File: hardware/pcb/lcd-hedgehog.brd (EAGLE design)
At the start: 24.4 x 27.4 mm, 40 parts

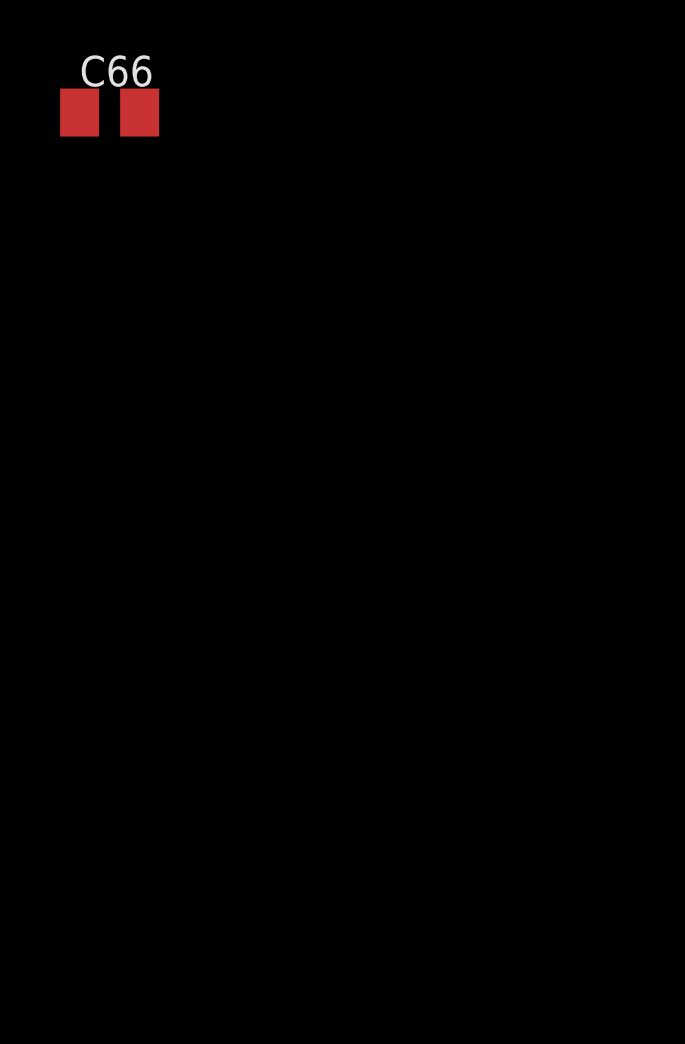
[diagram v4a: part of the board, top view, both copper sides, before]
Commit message: added 12V power circuit2
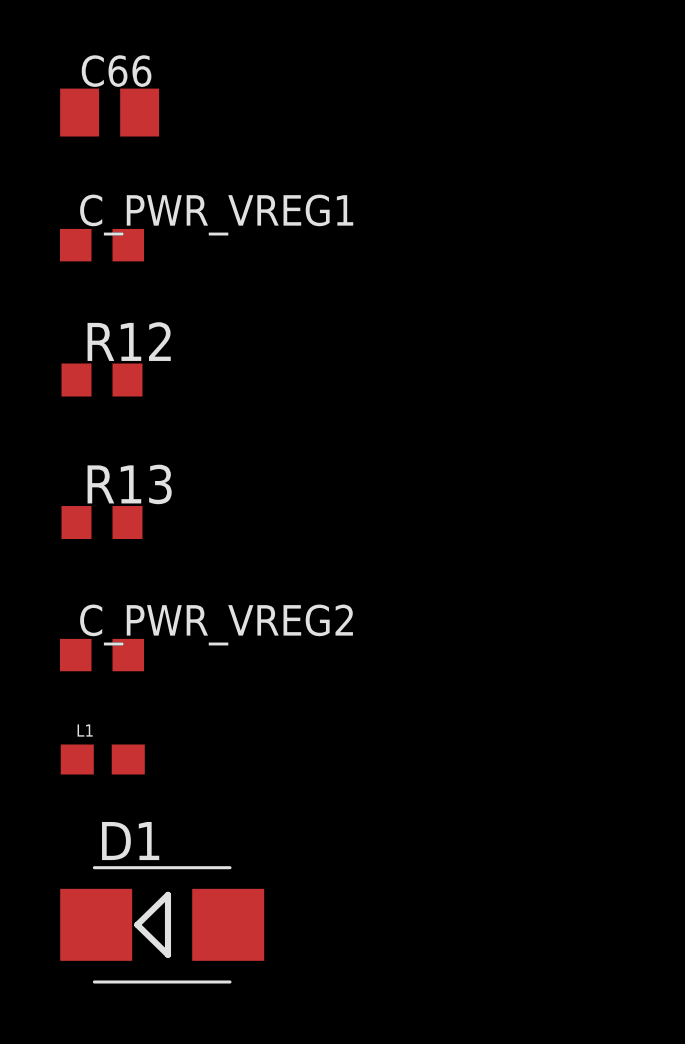
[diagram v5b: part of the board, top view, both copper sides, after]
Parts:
- added C_PWR_VREG1: 4.7uF, rcl:C0603K
- added C_PWR_VREG2: 1uF/12V, rcl:C0603K
- added D1: MBRS130LT3, diode:SMB
- added L1: 10uH, jnode:SPARKFUN_0603
- added R12: 27k, rcl:R0603
- added R13: 240k, rcl:R0603
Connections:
- new net 12V: C_PWR_VREG2.1, D1.C, R13.2, U$4.P$22
- new net N$15: R12.2, R13.1, U$5.3
- new net N$16: D1.A, L1.1, U$5.1
- net +3V3: now also C_PWR_VREG1.1, L1.2, U$5.4, U$5.5
- net GND: now also C_PWR_VREG1.2, C_PWR_VREG2.2, R12.1
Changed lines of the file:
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@@
 <element name="R11" library="rcl" package="R0603" value="20" x="-4.3942" y="-26.543"/>
 <element name="C66" library="rcl" package="C0805K" value="10uF" x="-4.1402" y="-31.1912"/>
+<element name="C_PWR_VREG1" library="rcl" package="C0603K" value="4.7uF" x="-4.3942" y="-35.6108"/>
+<element name="R12" library="rcl" package="R0603" value="27k" x="-4.3942" y="-40.1066"/>
+<element name="R13" library="rcl" package="R0603" value="240k" x="-4.3942" y="-44.8564"/>
+<element name="C_PWR_VREG2" library="rcl" package="C0603K" value="1uF/12V" x="-4.3942" y="-49.276"/>
+<element name="L1" library="jnode" package="SPARKFUN_0603" value="10uH" x="-4.3688" y="-52.7558"/>
+<element name="D1" library="diode" package="SMB" value="MBRS130LT3" x="-2.3876" y="-58.2676"/>
 </elements>
 <signals>
@@
 <contactref element="C64" pad="2"/>
 <contactref element="C66" pad="2"/>
+<contactref element="R12" pad="1"/>
+<contactref element="C_PWR_VREG2" pad="2"/>
+<contactref element="C_PWR_VREG1" pad="2"/>
+<wire x1="54.9402" y1="13.5722" x2="53.6702" y2="13.5722" width="0" layer="19" extent="1-1"/>
+<wire x1="34.1856" y1="16.8462" x2="53.6702" y2="13.5722" width="0" layer="19" extent="1-1"/>
 <wire x1="23.3172" y1="14.6812" x2="34.1856" y2="16.8462" width="0" layer="19" extent="1-1"/>
 <wire x1="19.4004" y1="13.684" x2="23.3172" y2="14.6812" width="0" layer="19" extent="1-1"/>
@@
 <wire x1="2.9808" y1="2.9232" x2="3.2512" y2="5.5786" width="0" layer="19" extent="1-16"/>
 <wire x1="1.524" y1="1.651" x2="2.9808" y2="2.9232" width="0" layer="19" extent="1-16"/>
-<wire x1="53.6702" y1="13.5722" x2="1.524" y2="1.651" width="0" layer="19" extent="1-1"/>
-<wire x1="54.9402" y1="13.5722" x2="53.6702" y2="13.5722" width="0" layer="19" extent="1-1"/>
 <wire x1="23.3473" y1="6.858" x2="19.4004" y2="9.684" width="0" layer="19" extent="1-1"/>
-<wire x1="-3.1402" y1="-17.145" x2="53.6702" y2="13.5722" width="0" layer="19" extent="1-1"/>
+<wire x1="-3.1402" y1="-17.145" x2="1.524" y2="1.651" width="0" layer="19" extent="1-1"/>
 <wire x1="-5.2442" y1="-26.543" x2="-3.1402" y2="-17.145" width="0" layer="19" extent="1-1"/>
 <wire x1="-3.1402" y1="-31.1912" x2="-5.2442" y2="-26.543" width="0" layer="19" extent="1-1"/>
+<wire x1="-3.5192" y1="-35.6108" x2="-3.1402" y2="-31.1912" width="0" layer="19" extent="1-1"/>
+<wire x1="-5.2442" y1="-40.1066" x2="-3.5192" y2="-35.6108" width="0" layer="19" extent="1-1"/>
+<wire x1="-3.5192" y1="-49.276" x2="-5.2442" y2="-40.1066" width="0" layer="19" extent="1-1"/>
 </signal>
 <signal name="D+">
@@
 <contactref element="C66" pad="1"/>
 <contactref element="U$2" pad="P9"/>
+<contactref element="C_PWR_VREG1" pad="1"/>
+<contactref element="U$5" pad="4"/>
+<contactref element="U$5" pad="5"/>
+<contactref element="L1" pad="2"/>
+<wire x1="49.8602" y1="7.4722" x2="54.9402" y2="7.4722" width="0" layer="19" extent="1-1"/>
+<wire x1="34.1856" y1="14.6462" x2="49.8602" y2="7.4722" width="0" layer="19" extent="1-1"/>
 <wire x1="19.4004" y1="14.184" x2="34.1856" y2="14.6462" width="0" layer="19" extent="1-1"/>
 <wire x1="19.4004" y1="9.184" x2="19.4004" y2="14.184" width="0" layer="19" extent="1-1"/>
-<wire x1="18.7604" y1="5.5508" x2="19.4004" y2="9.184" width="0" layer="19" extent="1-16"/>
-<wire x1="20.8026" y1="5.5508" x2="18.7604" y2="5.5508" width="0" layer="19" extent="16-16"/>
+<wire x1="20.7471" y1="7.808" x2="19.4004" y2="9.184" width="0" layer="19" extent="1-1"/>
+<wire x1="20.7471" y1="5.908" x2="20.7471" y2="7.808" width="0" layer="19" extent="1-1"/>
+<wire x1="20.8026" y1="5.5508" x2="20.7471" y2="5.908" width="0" layer="19" extent="1-16"/>
+<wire x1="18.7604" y1="5.5508" x2="20.7471" y2="5.908" width="0" layer="19" extent="1-16"/>
 <wire x1="13.9004" y1="8.184" x2="18.7604" y2="5.5508" width="0" layer="19" extent="1-16"/>
 <wire x1="10.8308" y1="10.9232" x2="13.9004" y2="8.184" width="0" layer="19" extent="1-16"/>
@@
 <wire x1="10.3496" y1="18.5928" x2="6.4262" y2="16.1408" width="0" layer="19" extent="1-1"/>
 <wire x1="8.4074" y1="21.7542" x2="10.3496" y2="18.5928" width="0" layer="19" extent="1-16"/>
-<wire x1="54.9402" y1="7.4722" x2="10.8308" y2="3.7232" width="0" layer="19" extent="1-16"/>
-<wire x1="49.8602" y1="7.4722" x2="54.9402" y2="7.4722" width="0" layer="19" extent="1-1"/>
-<wire x1="-3.5442" y1="-12.4968" x2="49.8602" y2="7.4722" width="0" layer="19" extent="1-1"/>
+<wire x1="-3.5442" y1="-12.4968" x2="0.9652" y2="7.3754" width="0" layer="19" extent="1-1"/>
 <wire x1="-5.1402" y1="-31.1912" x2="-3.5442" y2="-12.4968" width="0" layer="19" extent="1-1"/>
+<wire x1="-5.2692" y1="-35.6108" x2="-5.1402" y2="-31.1912" width="0" layer="19" extent="1-1"/>
+<wire x1="-3.5188" y1="-52.7558" x2="-5.2692" y2="-35.6108" width="0" layer="19" extent="1-1"/>
 </signal>
 <signal name="SDI">
@@
 <wire x1="-3.1402" y1="-21.7932" x2="-3.5442" y2="-26.543" width="0" layer="19" extent="1-1"/>
 </signal>
+<signal name="N$15">
+<contactref element="R12" pad="2"/>
+<contactref element="R13" pad="1"/>
+<contactref element="U$5" pad="3"/>
+<wire x1="-3.5442" y1="-40.1066" x2="-5.2442" y2="-44.8564" width="0" layer="19" extent="1-1"/>
+<wire x1="23.3473" y1="7.808" x2="-3.5442" y2="-40.1066" width="0" layer="19" extent="1-1"/>
+</signal>
+<signal name="12V">
+<contactref element="R13" pad="2"/>
+<contactref element="C_PWR_VREG2" pad="1"/>
+<contactref element="D1" pad="C"/>
+<contactref element="U$4" pad="P$22"/>
+<wire x1="-5.2692" y1="-49.276" x2="-4.5876" y2="-58.2676" width="0" layer="19" extent="1-1"/>
+<wire x1="-3.5442" y1="-44.8564" x2="-5.2692" y2="-49.276" width="0" layer="19" extent="1-1"/>
+<wire x1="6.7856" y1="4.556" x2="-3.5442" y2="-44.8564" width="0" layer="19" extent="1-1"/>
+</signal>
+<signal name="N$16">
+<contactref element="U$5" pad="1"/>
+<contactref element="D1" pad="A"/>
+<contactref element="L1" pad="1"/>
+<wire x1="-5.2188" y1="-52.7558" x2="-0.1876" y2="-58.2676" width="0" layer="19" extent="1-1"/>
+<wire x1="23.3473" y1="5.908" x2="-5.2188" y2="-52.7558" width="0" layer="19" extent="1-1"/>
+</signal>
 </signals>

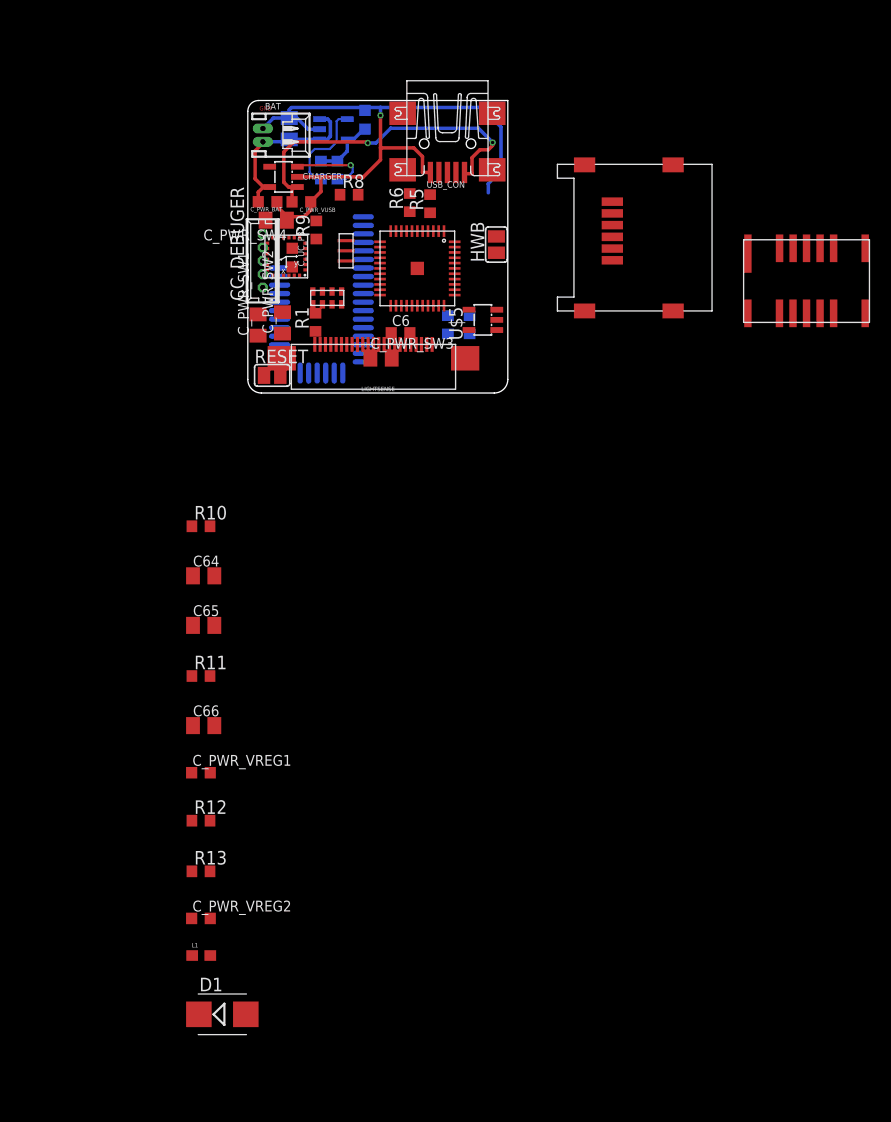
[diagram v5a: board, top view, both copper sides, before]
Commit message: connected Display & first placement
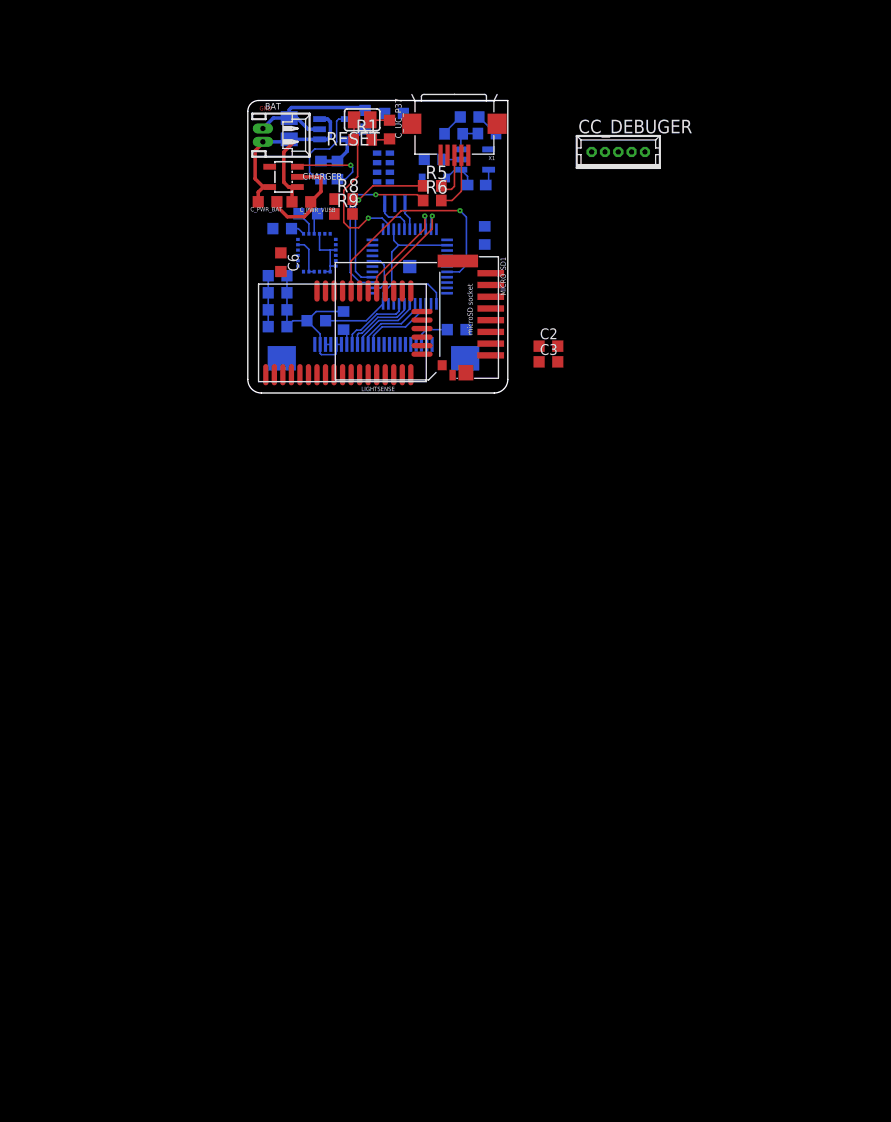
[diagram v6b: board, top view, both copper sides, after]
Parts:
- removed C64: 1.5uF, rcl:C0805K
- removed C65: 1uF, rcl:C0805K
- removed C66: 10uF, rcl:C0805K
- removed C_PWR_SW1, C_PWR_SW2: 10u, rcl:C0805K
- removed C_PWR_SW3: 4.7uF, rcl:C0805K
- removed C_PWR_SW4: 0.22uF, rcl:C0805K
- removed D1: MBRS130LT3, diode:SMB
- removed HWB: (no value), jumper:SJ
- removed R10, R2: 10k, rcl:R0603
- removed R11: 20, rcl:R0603
- removed SDCARD_CON: MICROSD_CONN, HedgehogLib:460DA40013
- removed USB_CON: USBCON, HedgehogLib:248601
- added 1.2M=((VIREF-GND)/IREF): 240k, rcl:R0603
- added C1, C3, C8, C_PWR_VUSB1, C_PWR_VUSB2: 10uF, rcl:C0603K
- added C10: 4.7uF, rcl:C0603K
- added C2, C5, C7: 0.1uF, rcl:C0603K
- added C4: 4.7uF/20V Tantalum CAP, rcl:C0603K
- added C9: 0.22uF, rcl:C0603K
- added MICRO_SD1: TECO_DIV_SENSOR_BOARD_MOLEX_47309-2651NEW, jnode_v32:TECO_DIV_SENSOR_BOARD_MOLEX_47309-2651
- added X1: SPARKFUN_USB-MICROB, jnode_v32:SPARKFUN_USB-MICROB
- U$2: value GRID-EYE -> DIODE-ZENER-BZT52; device HedgehogLib:GRID-EYE -> SparkFun-DiscreteSemi:SOD-323
- moved C_PWR_VREG2 79.3 mm to (20.8, 25.9), flipped to the bottom, turned to 180 degrees
- moved L1 76.7 mm to (21.5, 19.5), flipped to the bottom, turned to 180 degrees
- moved R13 73.1 mm to (19.3, 24.3), flipped to the bottom
- moved R12 69.8 mm to (22.4, 24.3), flipped to the bottom
- moved C_PWR_VREG1 61.5 mm to (17.4, 21.9), flipped to the bottom, turned to 180 degrees
- moved U$2 37.6 mm to (17.5, 20.2), flipped to the bottom, turned to 180 degrees
- moved CC_DEBUGER 34.9 mm to (34.7, 22.6), turned to 0 degrees
- moved RESET 25.4 mm to (10.7, 25.6), turned to 180 degrees
- moved R1 17.7 mm to (10.8, 23.7), turned to 0 degrees
- moved C_UC_P37 15.1 mm to (13.3, 24.7)
- moved U$5 15.1 mm to (21.3, 21.9), flipped to the bottom
- moved C6 13.0 mm to (3.10, 12.3), turned to 270 degrees
- moved U$3 12.7 mm to (12.7, 20.7), flipped to the bottom, turned to 90 degrees
- moved R4 9.06 mm to (22.2, 14.8)
- moved 12MHZ_RESONATOR 6.36 mm to (13.8, 17.8), flipped to the bottom, turned to 180 degrees
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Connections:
- removed net CS_SDCARD: R4.2, SDCARD_CON.P$2
- removed net GRID_EYE_INT: R10.1, U$2.P4
- removed net N$10: U$1.12
- removed net N$12: C64.1, U$2.P12
- removed net N$13: C65.1, U$2.P10
- removed net N$14: C65.2, R11.2
- removed net N$4: HWB.1, U$1.33
- removed net SDI: SDCARD_CON.P$3
- removed net SDO: R2.1, SDCARD_CON.P$7
- new net D_CS: U$1.41, U$4.P$8
- new net D_DC: U$1.39, U$4.P$10
- new net D_E: U$1.37, U$4.P$12
- new net D_POWER: U$1.36, U$5.4
- new net D_RES: U$1.40, U$4.P$9
- new net D_RW: U$1.38, U$4.P$11
- new net D_SCLK: U$4.P$13
- new net D_SDIN: U$4.P$14
- new net N$22: C4.2, U$4.P$21
- new net N$23: 1.2M=((VIREF-GND)/IREF).1, U$4.P$7
- new net SD_SEL: MICRO_SD1.2, U$1.12
- net +3V3: now also C1.1, C5.1, C7.1, C8.1, C_PWR_VUSB1.1, C_PWR_VUSB2.1, MICRO_SD1.4, U$4.P$3, U$4.P$4; no longer C66.1, C_PWR_SW1.2, C_PWR_SW2.2, R10.2, R2.2, SDCARD_CON.P$4, U$2.P13, U$2.P9, U$5.4
- net 12V: now also C2.1, C3.1, U$2.1; no longer D1.C
- net D+: now also X1.D+; no longer USB_CON.3
- net D-: now also X1.D-; no longer USB_CON.2
- net GND: now also 1.2M=((VIREF-GND)/IREF).2, C1.2, C10.1, C2.2, C3.2, C4.1, C5.2, C7.2, C8.2, C_PWR_VUSB1.2, C_PWR_VUSB2.2, MICRO_SD1.6, MICRO_SD1.CASE1, MICRO_SD1.CASE2, U$1.33, U$4.P$5, U$4.P$6, X1.GND, X1.GND@2, X1.GND@3; no longer C64.2, C66.2, C_PWR_SW1.1, C_PWR_SW2.1, C_PWR_SW3.2, HWB.2, R11.1, SDCARD_CON.P$6, U$2.P5, U$2.P6, USB_CON.5
- net MISO: now also MICRO_SD1.7, R4.2
- net MOSI: now also MICRO_SD1.3
- net N$16: now also U$2.2; no longer D1.A
- net N$7: now also C9.2; no longer C_PWR_SW4.1
- net N$8: now also C9.1; no longer C_PWR_SW4.2
- net N$9: now also C10.2; no longer C_PWR_SW3.1
- net SCL: no longer U$2.P3
- net SCLK: now also MICRO_SD1.5; no longer SDCARD_CON.P$5
- net SDA: no longer U$2.P2
- net V_USB: now also X1.VBUS; no longer USB_CON.1
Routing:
- net +3V3: track 6.03 -> 44.6 mm
- net P0_1/INT: track 0.00 -> 22.4 mm, vias 0 -> 1
- net V_USB: track 32.0 -> 11.3 mm, vias 2 -> 0
- net N$5: track 0.00 -> 16.5 mm, vias 0 -> 1
- net N$1: track 0.00 -> 15.8 mm, vias 0 -> 1
- net N$6: track 0.00 -> 15.2 mm, vias 0 -> 1
- net GND: track 63.7 -> 52.8 mm, vias 1 -> 0
- net P0_4/TX: track 0.00 -> 10.2 mm, vias 0 -> 1
- net P0_5/RX: track 0.00 -> 10.1 mm, vias 0 -> 1
- net D_E: track 0.00 -> 6.92 mm
- net D_CS: track 0.00 -> 6.92 mm
- net D_RES: track 0.00 -> 6.86 mm
- net D_RW: track 0.00 -> 6.74 mm
- net D_DC: track 0.00 -> 6.68 mm
- net D-: track 0.00 -> 5.62 mm
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
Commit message: updated brd
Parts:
- moved CC_DEBUGER 17.7 mm to (19.2, 31.2)
- moved C6 6.59 mm to (9.67, 11.8), turned to 180 degrees
- moved C8 0.90 mm to (2.79, 10.1)
- moved C5 0.70 mm to (2.79, 8.70)
- moved R5 0.70 mm to (17.3, 20.1)
- moved C1 0.50 mm to (2.79, 7.30)
- moved R6 0.30 mm to (17.3, 18.4)
- moved C7 0.30 mm to (2.79, 5.92)
- moved R4 0.08 mm to (22.3, 14.8), turned to 270 degrees
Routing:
- net +3V3: track 44.6 -> 119.1 mm, vias 0 -> 5
- net V_USB: track 11.3 -> 61.5 mm, vias 0 -> 1
- net 12V: track 2.19 -> 48.0 mm, vias 0 -> 2
- net SDA: track 0.00 -> 37.6 mm, vias 0 -> 2
- net SCL: track 0.00 -> 25.8 mm, vias 0 -> 2
- net D_POWER: track 0.00 -> 23.3 mm
- net 3G_INT: track 0.00 -> 22.2 mm, vias 0 -> 2
- net SD_SEL: track 0.00 -> 20.0 mm, vias 0 -> 1
- net MISO: track 0.00 -> 17.5 mm, vias 0 -> 2
- net MOSI: track 0.00 -> 16.8 mm, vias 0 -> 1
- net SCLK: track 0.00 -> 13.3 mm, vias 0 -> 1
- net GND: track 52.8 -> 61.8 mm, vias 0 -> 10
- net BLE_RESET: track 0.00 -> 8.95 mm
- net POK: track 7.49 -> 4.46 mm
- net P0_5/RX: track 10.1 -> 12.2 mm
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- added copper zone on layer 1, net GND
- added copper zone on layer 16, net GND
